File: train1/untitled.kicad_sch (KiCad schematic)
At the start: 33 parts, among them J1 DC5521/2.1mm, Q6 SI2301/SOT23-3, U1 XL1509-5.0E1, U2 AMS1117-3.3

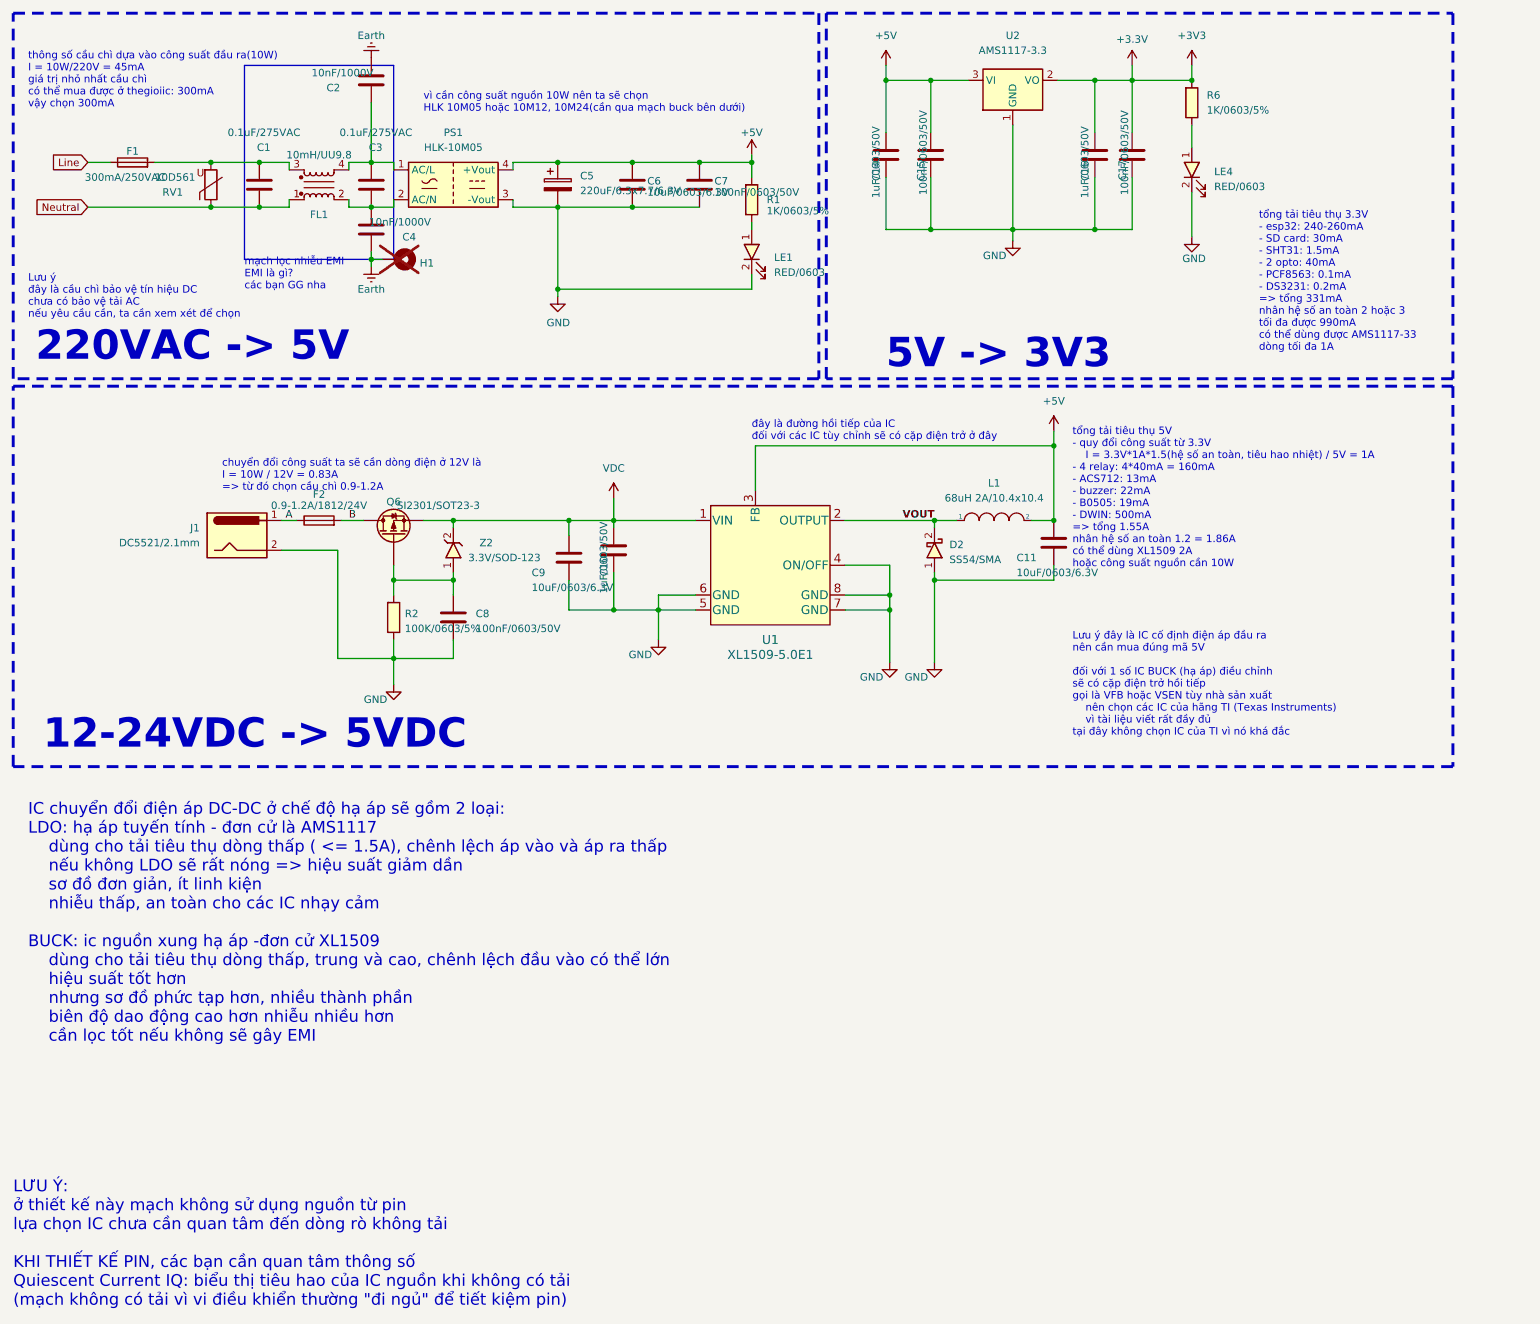
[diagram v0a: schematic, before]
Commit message: fix(repo): delete backup file
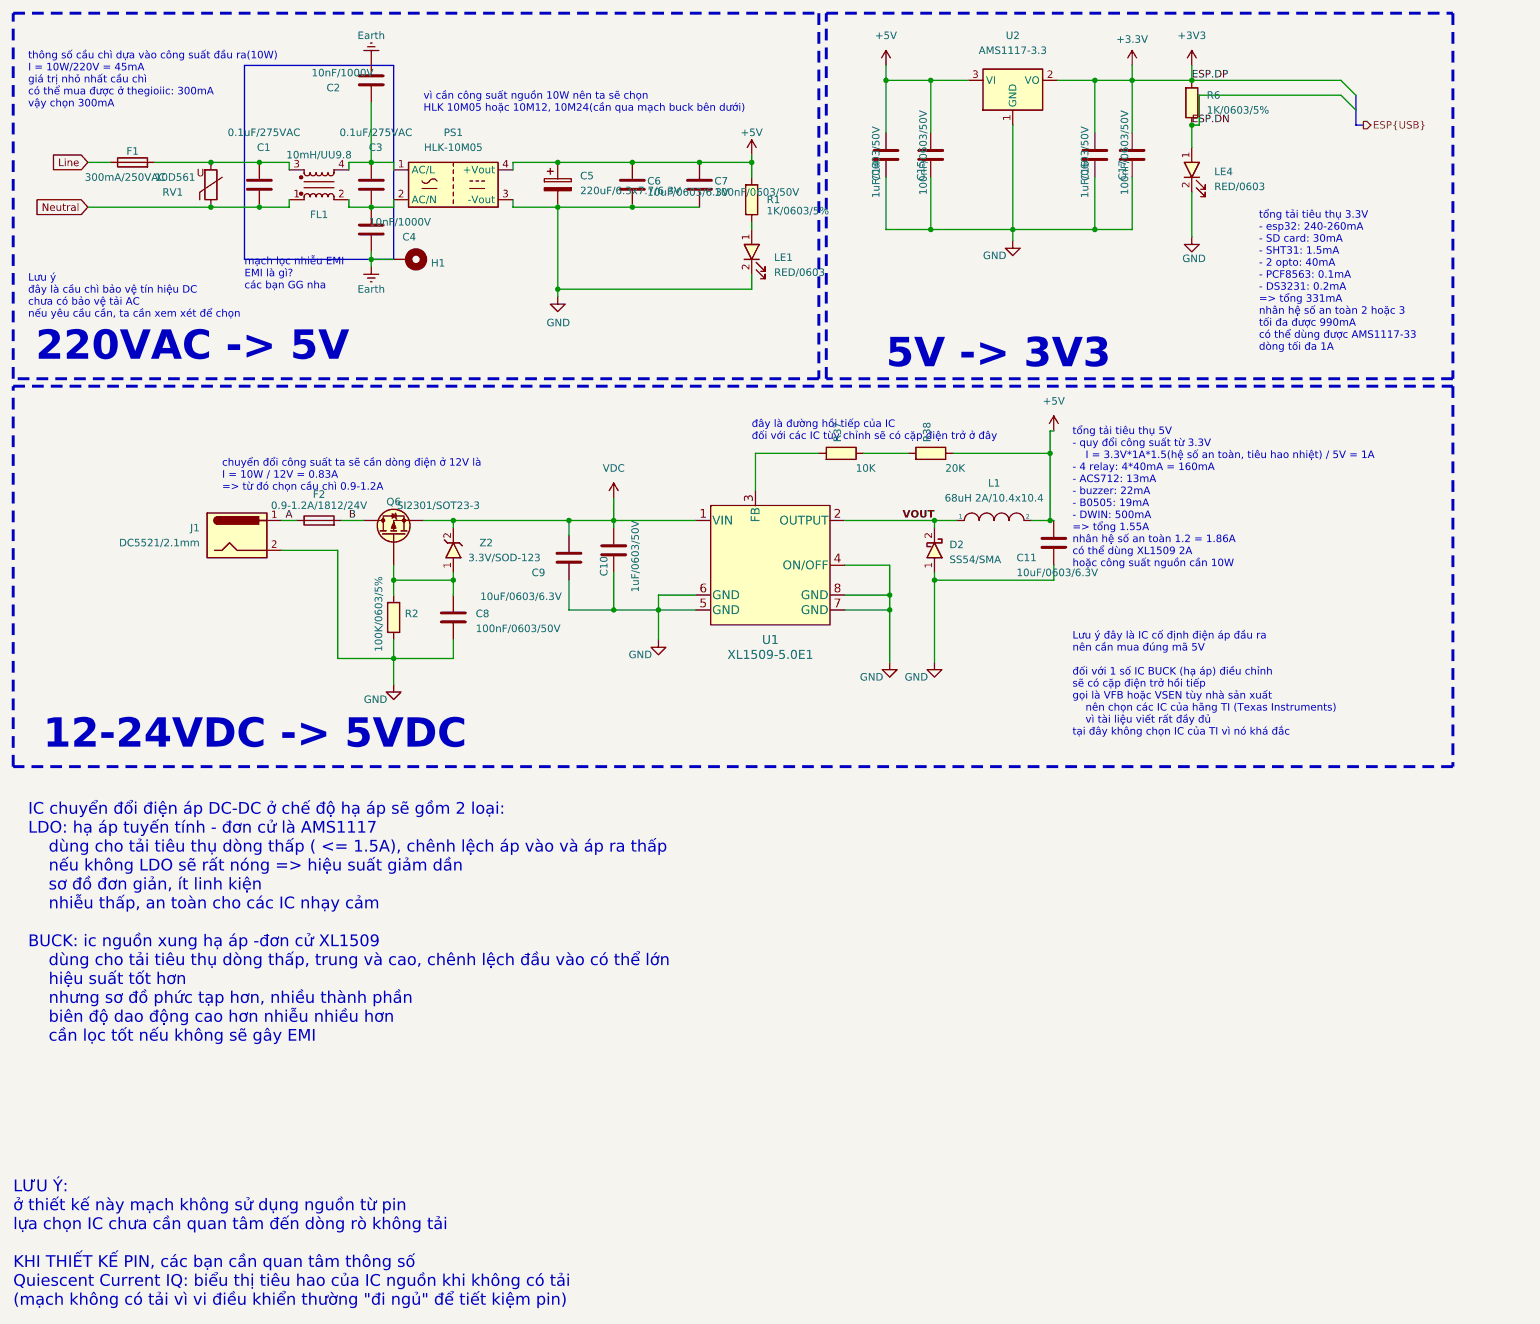
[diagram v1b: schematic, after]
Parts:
- added R37: 10K, trainFootprint:C_0603, symbol TrainSymbol:R
- added R38: 20K, trainFootprint:C_0603, symbol TrainSymbol:R
- H1: now fitted
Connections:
- net +5V: now also R38.2; no longer U1.3 (FB)
- net ESP.DN: now reaches LE4.1, R6.2
- new net: R37.1, U1.3 (FB)
- new net: R37.2, R38.1
